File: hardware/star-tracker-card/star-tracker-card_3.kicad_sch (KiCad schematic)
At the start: 140 parts, among them J100 DM3BT-DSF-PEJS, J101 3-1734592-64-1734592-0, J3 CONN_03LONGPADS, U11 TCAN330, U17 25AAXX, U3 THGBMJG7C2LBAU8, U5 SN74LVC8T245MPWREPPW24-M, U6 CLVCH16T245MDGGREP, U7 OSD3358-512M-BSM, U8 TLV70028QDDCRQ1, U9 TCA9509DGKRDGK8-M

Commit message: More EAGLE import cleanup
Fixed sheets, did some ERC cleanup, imported into layout, impmorted 4 layer DRC rules.
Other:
- note removed: "1.2"
- note removed: "OreSat Star Tracker: Camera, eMMC"
- company: (none) -> Portland State Aerospace Society
- title: (none) -> OreSat Star Tracker

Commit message: Schematic Overhaul of v1.3
Changed schematic to hierarchical, changed debug connector, updated OPD, removed JTAG, and ESD protection on removed connectors
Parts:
- removed C16, C17, C20, C21, C24, C25, C26, C28: 0.1uF, star-tracker-card:.0603-A, symbol star-tracker-card-eagle-import:C-EU0603-A
- removed C23, C27: 1uF, star-tracker-card:.0603-A, symbol star-tracker-card-eagle-import:C-EU0603-A
- removed C42, C43: 22uF, star-tracker-card:C1210, symbol star-tracker-card-eagle-import:C-EUC1210
- removed J101: 3-1734592-64-1734592-0, star-tracker-card:TE_3-1734592-6, symbol star-tracker-card-eagle-import:3-1734592-64-1734592-0
- removed J3: CONN_03LONGPADS, star-tracker-card:1X03_LONGPADS, symbol star-tracker-card-eagle-import:CONN_03LONGPADS
- removed JP105, JP106, JP108, JP109: JUMPER-SMT_3_1-NC_TRACE_SILK, star-tracker-card:SMT-JUMPER_3_1-NC_TRACE_SILK, symbol star-tracker-card-eagle-import:JUMPER-SMT_3_1-NC_TRACE_SILK
- removed JP107: JUMPER-SMT_3_NO_SILK, star-tracker-card:SMT-JUMPER_3_NO_SILK, symbol star-tracker-card-eagle-import:JUMPER-SMT_3_NO_SILK
- removed R11, R12, R14, R16, R21: 10k, star-tracker-card:.0603-A, symbol star-tracker-card-eagle-import:R-US_0603-A
- removed R17, R18: 4.7k, star-tracker-card:.0603-A, symbol star-tracker-card-eagle-import:R-US_0603-A
- removed R24, R25, R26: 100K, star-tracker-card:ARRAY_EXBA-M, symbol star-tracker-card-eagle-import:EXB-A10P391JC_ARRAY_EXBA-M
- removed TP10, TP11, TP113, TP116, TP119, TP12, TP13, TP135, TP137, TP143, TP147, TP148, TP149, TP15, TP152, TP153, TP158, TP159, TP16, TP162, TP17, TP174, TP18, TP19, TP20, TP21, TP23, TP24, TP26, TP27, TP28, TP29, TP36, TP37, TP5, TP6, TP7, TP8, TP9: TEST-POINT3X4, star-tracker-card:PAD.03X.04, symbol star-tracker-card-eagle-import:TEST-POINT3X4
- removed U5: SN74LVC8T245MPWREPPW24-M, star-tracker-card:PW24-M, symbol star-tracker-card-eagle-import:SN74LVC8T245MPWREPPW24-M
- removed U6: CLVCH16T245MDGGREP, star-tracker-card:DGG48-M, symbol star-tracker-card-eagle-import:CLVCH16T245MDGGREP
- removed unit 4 of U7
- removed U8: TLV70028QDDCRQ1, star-tracker-card:SOT23-5, symbol star-tracker-card-eagle-import:TLV70028QDDCRQ1
- removed U9: TCA9509DGKRDGK8-M, star-tracker-card:DGK8-M, symbol star-tracker-card-eagle-import:TCA9509DGKRDGK8-M
- C10, C11, C12, C3, C31, C40, C5, C6, C9: footprint star-tracker-card:.0603-A -> oresat-passives:c_0603-SMALL; symbol star-tracker-card-eagle-import:C-EU0603-A -> Device:C_Small
- C2: footprint star-tracker-card:.0805-B -> oresat-passives:0805-B-NOSILK; symbol star-tracker-card-eagle-import:C-EU0805-B -> Device:C_Small
- C8: footprint star-tracker-card:.0805-B -> oresat-passives:0805-B-NOSILK
- D2, D3, D4, D5: symbol star-tracker-card-eagle-import:LED-BLUE0603 -> Device:LED
- R2, R29, R3, R30, R4, R5, R60: footprint star-tracker-card:.0603-A -> Resistor_SMD:R_0603_1608Metric; symbol star-tracker-card-eagle-import:R-US_0603-A -> Device:R_Small_US
- R59: footprint star-tracker-card:.0603-A -> Resistor_SMD:R_0603_1608Metric; symbol star-tracker-card-eagle-import:R-US_0603-A -> Device:R_Small_US; now not fitted
- TP100, TP101, TP103, TP104, TP105, TP106, TP107, TP108, TP111, TP114, TP115, TP117, TP118, TP120, TP122, TP123, TP124, TP125, TP126, TP127, TP128, TP131, TP134, TP142, TP146, TP177, TP178, TP180, TP22, TP30, TP35, TP40, TP69: footprint star-tracker-card:PAD.03X.04 -> oresat-misc:TestPoint_Pad_D1.0mm; symbol star-tracker-card-eagle-import:TEST-POINT3X4 -> oresat-misc:Test-Point-1mm-round; now left out of the parts list
- U11: footprint star-tracker-card:SOT23-8_TI-DCN -> oresat-live-card:SOT23-8_TI-DCN; symbol star-tracker-card-eagle-import:TCAN330 -> oresat-ics:TCAN330; Distributor (none) -> DigiKey; MPN (none) -> TCAN330GDCN
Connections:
- net GND: now also D2.1 (K), D3.1 (K), D4.1 (K), D5.1 (K); no longer D2.C, D3.C, D4.C, D5.C
- net UART0_RX: now also TP146.1; no longer TP146.P$1 (1)
- net UART0_TX: now also TP142.1; no longer TP142.P$1 (1)
- net at R2.2: now also D2.2 (A); no longer D2.A
- net at U7.N1 (GPMC_OEN_REN): now also TP128.1; no longer TP128.P$1 (1)
- net at U7.P15 (GPMC_WAIT0): now also TP114.1; no longer TP114.P$1 (1)
- net at U7.T15 (GPMC_A9): now also TP108.1; no longer TP108.P$1 (1)
- net at U7.N14 (GPMC_BEN1): now also TP125.1; no longer TP125.P$1 (1)
- net at U7.A4 (XDMA_EVENT_INTR0): now also TP30.1; no longer TP30.P$1 (1)
- net at U7.C12 (UART0_CTSN): now also TP177.1; no longer TP177.P$1 (1)
- net at U7.C13 (UART0_RTSN): now also TP178.1; no longer TP178.P$1 (1)
- net at J100.CD (CD#), R8.6 (66), U7.C14 (SPI0_CS1): now also TP22.1; no longer TP22.P$1 (1)
- net at U7.C5 (ECAP0_IN_PWM0_OUT): now also TP180.1; no longer TP180.P$1 (1)
- net at U7.M1 (GPMC_ADVN_ALE): now also TP134.1; no longer TP134.P$1 (1)
- net at U7.N2 (GPMC_WEN): now also TP127.1; no longer TP127.P$1 (1)
- net at U7.N3 (GPMC_BEN0_CLE): now also TP131.1; no longer TP131.P$1 (1)
- net at U7.P12 (GPMC_A2): now also TP126.1; no longer TP126.P$1 (1)
- net at U7.P3 (GPMC_CSN0): now also TP122.1; no longer TP122.P$1 (1)
- net at U7.P5 (GPMC_AD9): now also TP123.1; no longer TP123.P$1 (1)
- net at U7.P6 (GPMC_AD12): now also TP124.1; no longer TP124.P$1 (1)
- net at U7.R12 (GPMC_A1): now also TP118.1; no longer TP118.P$1 (1)
- net at U7.R15 (GPMC_A10): now also TP117.1; no longer TP117.P$1 (1)
- net at U7.R16 (GPMC_WPN): now also TP111.1; no longer TP111.P$1 (1)
- net at U7.R5 (GPMC_AD10): now also TP115.1; no longer TP115.P$1 (1)
- net at U7.R6 (GPMC_AD13): now also TP120.1; no longer TP120.P$1 (1)
- net at U7.R7 (GPMC_CSN3): now also TP107.1; no longer TP107.P$1 (1)
- net at U7.T12 (GPMC_A0): now also TP100.1; no longer TP100.P$1 (1)
- net at U7.T13 (GPMC_A3): now also TP101.1; no longer TP101.P$1 (1)
- net at U7.T16 (GPMC_A11): now also TP103.1; no longer TP103.P$1 (1)
- net at U7.T4 (GPMC_AD8): now also TP104.1; no longer TP104.P$1 (1)
- net at U7.T5 (GPMC_AD11): now also TP105.1; no longer TP105.P$1 (1)
- net at U7.T7 (GPMC_CLK): now also TP106.1; no longer TP106.P$1 (1)
- net at R4.2: now also D4.2 (A); no longer D4.A
- net at R3.2: now also D3.2 (A); no longer D3.A
- net at R5.2: now also D5.2 (A); no longer D5.A
- net at U11.5 (SHDN): now also TP35.1; no longer TP35.P$1 (1)
- net at U11.8 (S): now also TP40.1; no longer TP40.P$1 (1)
- net at U17.7 (~{HOLD}): now also TP69.1; no longer TP69.P$1 (1)
- net VSYNC_I renamed VSYNCI
- no-connect marks 11 -> 6
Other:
- note removed: "2.8V regulator"
- note removed: "36 Pin connector"
- note removed: "Boot SD SYSBOOT[4 : 0] == 0b11000 SPI0 -> MMC0 -> USB0 -> UART0 Boot eMMC SYSBOOT[4 : 0] == 0b11100 MMC1 -> MMC0 -> UART0 -> USB0"
- note removed: "Camera Control Level Shifter"
- note removed: "Camera Output Level Shifter"
- note removed: "Default Sysboot Pins SYSBOOT[4 : 0] == 0b11x00 SYSBOOT[2] HIGH == eMMC SYSBOOT[2] LOW == SD Card"
- note removed: "GPIO -> PIN map gpio3_9 == mii1_tx_clk gpio0_28 == mii1_txd0 gpio0_21 == mii1_txd1 gpio0_17 == mii1_txd2 gpio0_16 == mii1_txd3 gpio3_3 == mii1_tx_en gpio3_1 == mii1_crs gpio3_0 == mii1_col gpio3_10 == mii1_rx_clk gpio2_21 == mii1_rxd0 gpio2_20 == mii1_rxd1 gpio2_19 == mii1_rxd2 gpio2_18 == mii1_rxd3 gpio3_2 == mii1_rx_er gpio3_4 == mii1_rx_dv gpio0_0 == mdio"
- note removed: "I2C Transceiver"
- note removed: "NOTE: All these signals are outputs with the exception of FLASH. Likewise, I put the outputs on GPIO2,3 and inputs on GPIO0. I am not sure if this is better, but it seemed logical"
- note removed: "OE pullup to start in high Z"
- note removed: "SYSBOOT Circuit"
- note removed: "SYSBOOT Jumper to config boot order must use very light pullups because boot config is latched at boot and then the pins a used for other purposes"
- note removed: "SYSBOOT[15 : 5] == 0b0100_0000_000"
- note removed: "These pullups can be populated instead of the optional ones on the camera board"
- moved on the sheet: C8, JP102, JP103, JP110, JP111, R10, R8, R9

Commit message: Update
Update to the octavo schematic
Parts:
- removed JP102, JP103, JP110, JP111: JUMPER-SMT_3_1-NC_TRACE_SILK, star-tracker-card:SMT-JUMPER_3_1-NC_TRACE_SILK, symbol star-tracker-card-eagle-import:JUMPER-SMT_3_1-NC_TRACE_SILK
- C8: symbol star-tracker-card-eagle-import:C-EU0805-B -> Device:C_Small
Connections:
- net D0_I: now also J100.2 (DAT3/CS), R8.2 (22), U7.C15 (MMC0_DAT3)
- net D1_I: now also J100.1 (DAT2), R8.9 (99), U7.C16 (MMC0_DAT2)
- net D2_I: now also J100.8 (DAT1), R8.4 (44), U7.A15 (MMC0_DAT1)
- net D3_I: now also J100.7 (DAT0/DO), R8.7 (77), U7.A16 (MMC0_DAT0)
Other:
- note removed: "SD Card Circuit pinout from RED board"
- moved on the sheet: C11

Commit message: DRC hunting
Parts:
- D2, D3, D4, D5: footprint star-tracker-card:LED-0603 -> LED_SMD:LED_0603_1608Metric
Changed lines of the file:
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@@
 			)
 		)
-		(property "Footprint" "star-tracker-card:LED-0603"
+		(property "Footprint" "LED_SMD:LED_0603_1608Metric"
 			(at 382.27 195.58 0)
 			(effects
@@
 			)
 		)
-		(property "Footprint" "star-tracker-card:LED-0603"
+		(property "Footprint" "LED_SMD:LED_0603_1608Metric"
 			(at 382.27 210.82 0)
 			(effects
@@
 			)
 		)
-		(property "Footprint" "star-tracker-card:LED-0603"
+		(property "Footprint" "LED_SMD:LED_0603_1608Metric"
 			(at 382.27 203.2 0)
 			(effects
@@
 			)
 		)
-		(property "Footprint" "star-tracker-card:LED-0603"
+		(property "Footprint" "LED_SMD:LED_0603_1608Metric"
 			(at 382.27 218.44 0)
 			(effects

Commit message: Big almost-done cleanup
Fixed a bunch of things in the schematic. Compared against C3 Octavo. Fixed all weird ERCs. Cleaned up a lot of planes on the layout. Moved uart switch, rerouted a bunch of traces for better layout. Fixed library issues, and board/sch sync issues.
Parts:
- removed C40: 0.1uF, oresat-passives:c_0603-SMALL, symbol Device:C_Small
- removed R59, R60: DNP, Resistor_SMD:R_0603_1608Metric, symbol Device:R_Small_US
- removed TP22, TP35, TP40, TP69: TEST-POINT3X4, oresat-misc:TestPoint_Pad_D1.0mm, symbol oresat-misc:Test-Point-1mm-round
- removed U17: 25AAXX, star-tracker-card:SOIC8, symbol star-tracker-card-eagle-import:25AAXX
- added TP1, TP14, TP2, TP31: TEST-POINT3X4, oresat-misc:TestPoint_Pad_D1.0mm, symbol oresat-misc:Test-Point-1mm-round
- C10, C12, C3, C5, C6, C9: value 1uF -> 1u; footprint oresat-passives:c_0603-SMALL -> oresat-passives:0603-C-NOSILK
- C11, C31: value 0.1uF -> 100n; footprint oresat-passives:c_0603-SMALL -> oresat-passives:0603-C-NOSILK
- C2, C8: value 10uF -> 10u
- D2, D3, D4, D5: value BLUE -> BLU; symbol Device:LED -> Device:LED_Small_Filled
- R2, R29, R3, R30, R4, R5: footprint Resistor_SMD:R_0603_1608Metric -> oresat-passives:0603-C-NOSILK
- U11: footprint oresat-live-card:SOT23-8_TI-DCN -> Package_TO_SOT_SMD:SOT-23-8; symbol oresat-ics:TCAN330 -> Interface_CAN_LIN:TCAN330
- U3: value THGBMJG7C2LBAU8 -> EMMC+RESET+5.1-COMPATIBLE-BA; footprint star-tracker-card:BGA-153(11.5X13)(EMMC-BA) -> oresat-ics:BGA-153(11.5X13)(EMMC-BA); symbol star-tracker-card-eagle-import:EMMC+RESET+5.1-COMPATIBLE-BA -> oresat-ics:EMMC+RESET+5.1-COMPATIBLE-BA
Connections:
- net GND: now also U3.A6 (VSSIO)
- net EMMC_CMD: now reaches R9.2 (22), U3.M5 (CMD), U7.P1 (GPMC_CSN2)
- net EMMC_D5: now reaches R9.3 (33), U3.B4 (D5), U7.T1 (GPMC_AD5)
- net EMMC_D4: now reaches R9.4 (44), U3.B3 (D4), U7.T2 (GPMC_AD4)
- net EMMC_D0: now reaches R9.6 (66), U3.A3 (D0), U7.R3 (GPMC_AD0)
- net EMMC_D3: now reaches R9.7 (77), U3.B2 (D3), U7.T3 (GPMC_AD3)
- net EMMC_SCK: now reaches R9.8 (88), U3.M6 (SCK), U7.P2 (GPMC_CSN1)
- net CAN1_TXD: now reaches U11.1 (TXD), U7.A11 (UART1_RXD)
- net at U7.A13 (SPI0_SCLK): now also TP1.1
- net at U7.A14 (SPI0_CS0): now also TP31.1
- net CAN1_RXD: now reaches U11.4 (RXD), U7.B11 (UART1_TXD)
- net at U7.B13 (SPI0_D0): now also TP2.1
- net at U7.B14 (SPI0_D1): now also TP14.1
- net MMC1_CLK: now reaches J100.5 (CLK), R8.3 (33), U7.B15 (MMC0_CLK)
- net MMC1_CMD: now reaches J100.3 (CMD/DI), R8.8 (88), U7.B16 (MMC0_CMD)
- net MMC1_CD: now reaches J100.CD (CD#), R8.6 (66), U7.C14 (SPI0_CS1)
- net EMMC_D6: now reaches R10.8 (88), U3.B5 (D6), U7.P4 (GPMC_AD6)
- net EMMC_D2: now reaches R10.9 (99), U3.A5 (D2), U7.R1 (GPMC_AD2)
- net EMMC_nRST: now reaches R10.3 (33), U3.K5 (~{RST}), U7.R13 (GPMC_A4)
- net EMMC_D1: now reaches R10.1 (11), U3.A4 (D1), U7.R2 (GPMC_AD1)
- net EMMC_D7: now reaches R10.2 (22), U3.B6 (D7), U7.R4 (GPMC_AD7)
- no-connect marks 6 -> 8
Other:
- note added: "0805"
- note added: "All resistors are 0603 1% AEC-Q200 unless marked. All capacitors are 0603 AEC-Q200 Vw >= 16V X5R or better unless marked."
- note added: "Need ~2.2uF, using two 1uF for simplicity"
- note removed: "CAN Transceiver"
- note removed: "CAN1 RX --> B11 --> UART1_TXD CAN1 TX --> A11 --> UART1_RXD"
- note removed: "Camera Connector and Circuitry"
- note removed: "I2C2 SCL == UART1_RTSN == A10 I2C2 SDA == UART1_CTSN == B10"
- note removed: "Need ~2.2uF here, but using two 1uF for simplicity"
- note removed: "SPI Flash/EEPROM For SPI boot DNP for now"
- moved on the sheet: C10, C11, C12, C2, C3, C31, C5, C6, C8, C9, J100, R10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

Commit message: BOM 99% completed, push for final review
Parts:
- C10, C12, C3, C5, C6, C9: DIS (none) -> DigiKey; DPN (none) -> 490-GRT188R71E105KE13DCT-ND; MFR (none) -> Murata Electronics; MPN (none) -> GRT188R71E105KE13D
- C11, C31: DIS (none) -> DigiKey; DPN (none) -> 399-6856-1-ND; MFR (none) -> KEMET; MPN (none) -> C0603C104K5RACAUTO
- C2, C8: DIS (none) -> DigiKey; DPN (none) -> 490-GRT21BC71E106KE13KCT-ND; MFR (none) -> Murata Electronics; MPN (none) -> GRT21BC71E106KE13K
- D2, D3, D4, D5: DIS (none) -> DigiKey; DPN (none) -> 732-4966-1-ND; MFR (none) -> Wurth; MPN (none) -> 150060BS75000
- J100: DIS (none) -> DigiKey; DPN (none) -> HR1942CT-ND; MFR (none) -> Hirose; MPN (none) -> DM3BT-DSF-PEJS
- R10, R8, R9: DIS (none) -> DigiKey; DPN U7103CT-ND -> RMCF0603FT10K0CT-ND; MFR (none) -> Stackpole Electronics; MPN EXB-A10P103J -> RMCF0603FT10K0
- R2, R3, R4, R5: DIS (none) -> DigiKey; DPN (none) -> RMCF0603FT2K70CT-ND; MFR (none) -> Stackpole Electronics; MPN (none) -> RMCF0603FT1K00
- R29, R30: DIS (none) -> DigiKey; DPN (none) -> RMCF0603FT4K70CT-ND; MFR (none) -> Stackpole Electronics; MPN (none) -> RMCF0603FT4K70
- U11: DIS (none) -> DigiKey; DPN (none) -> 296-44211-1-ND; MFR (none) -> Texas Instruments
- U3: DIS (none) -> DigiKey; DPN THGBMJG7C2LBAU8-ND -> 1052-SFEM016GB1EA1TO-I-GE-121-STD-ND; MFR (none) -> Swissbit; MPN THGBMJG7C2LBAU8 -> SFEM016GB1EA1TO-I-GE-121-STD
- U7: DIS (none) -> DigiKey; DPN (none) -> 1676-OSD3358-1G-ISM-ND; MFR (none) -> Octavo Systems LLC; MPN (none) -> OSD3358-1G-ISM

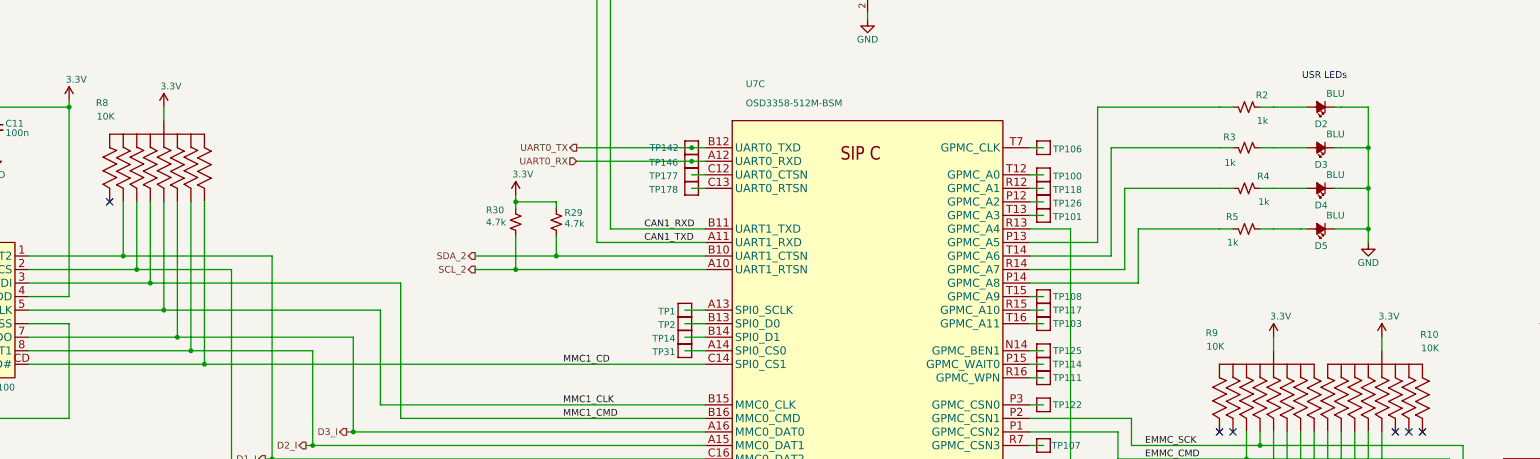
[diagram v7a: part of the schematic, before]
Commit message: Star Tracker v1.3 files, including new Makefile, Readme, and fixes in ERC, DRC, and layout
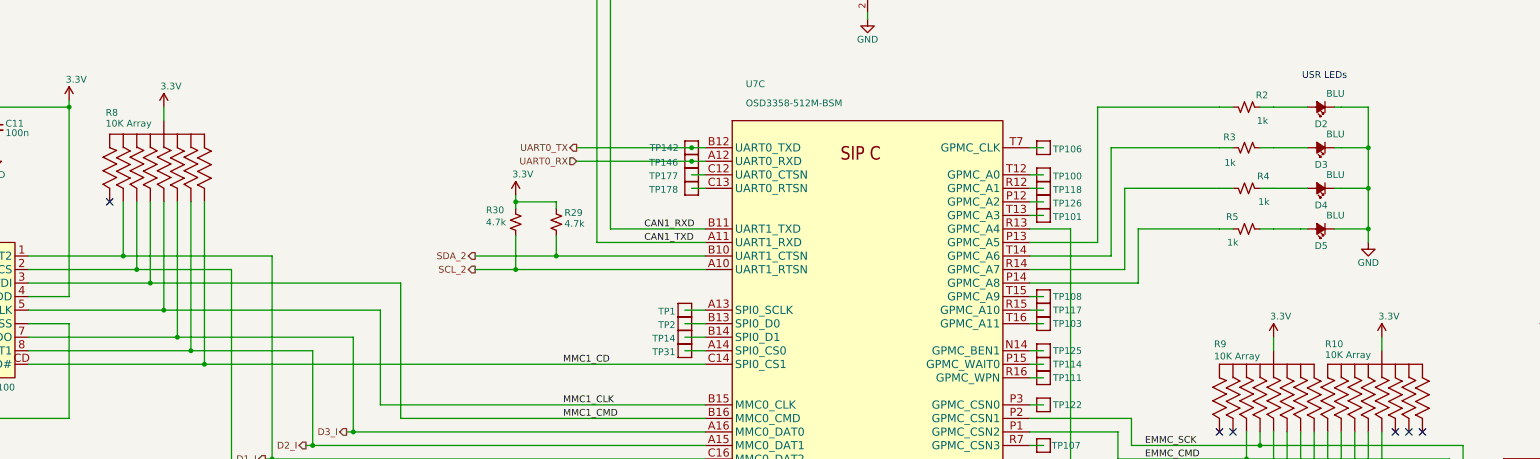
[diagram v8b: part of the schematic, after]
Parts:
- R10, R8, R9: value 10K -> 10K Array; DPN RMCF0603FT10K0CT-ND -> U7103CT-ND; MFR Stackpole Electronics -> Panasonic Electronic Components; MPN RMCF0603FT10K0 -> EXB-A10P103J
- U11: Distributor DigiKey -> (none)
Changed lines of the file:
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@@
 	(title_block
 		(title "OreSat Star Tracker")
-		(date "2026-04-15")
+		(date "2026-04-22")
 		(rev "1.3")
 		(company "Portland State Aerospace Society")
@@
 		(dnp no)
 		(property "Reference" "R9"
-			(at 275.5392 126.9492 90)
+			(at 277.114 129.032 90)
 			(show_name no)
 			(do_not_autoplace no)
@@
 			)
 		)
-		(property "Value" "10K"
-			(at 275.6916 129.4892 90)
+		(property "Value" "10K Array"
+			(at 277.114 131.318 90)
 			(show_name no)
 			(do_not_autoplace no)
@@
 			)
 		)
-		(property "Datasheet" "https://www.seielect.com/catalog/SEI-RMCF_RMCP.pdf"
+		(property "Datasheet" "https://industrial.panasonic.com/ww/products/pt/resistor-network-array/models/EXBA10P103J"
 			(at 278.13 132.08 0)
 			(hide yes)
@@
 			)
 		)
-		(property "Description" "10 kOhms ±1% 0.1W, 1/10W Chip Resistor 0603 (1608 Metric) Automotive AEC-Q200 Thick Film"
+		(property "Description" "10k Ohm ±5% 62.5mW Power Per Element Bussed 8 Resistor Network/Array ±200ppm/°C 2512 (6432 Metric), Concave, Long Side Terminals"
 			(at 278.13 132.08 0)
 			(hide yes)
@@
 			)
 		)
-		(property "DPN" "RMCF0603FT10K0CT-ND"
+		(property "DPN" "U7103CT-ND"
 			(at 278.13 132.08 0)
 			(hide yes)
@@
 			)
 		)
-		(property "MPN" "RMCF0603FT10K0"
+		(property "MPN" "EXB-A10P103J"
 			(at 278.13 132.08 0)
 			(hide yes)
@@
 			)
 		)
-		(property "MFR" "Stackpole Electronics"
+		(property "MFR" "Panasonic Electronic Components"
 			(at 278.13 132.08 90)
 			(hide yes)
@@
 		(dnp no)
 		(property "Reference" "R8"
-			(at 67.2592 83.7692 90)
+			(at 69.088 85.598 90)
 			(show_name no)
 			(do_not_autoplace no)
@@
 			)
 		)
-		(property "Value" "10K"
-			(at 67.4116 86.3092 90)
+		(property "Value" "10K Array"
+			(at 69.088 87.63 90)
 			(show_name no)
 			(do_not_autoplace no)
@@
 			)
 		)
-		(property "Datasheet" "https://www.seielect.com/catalog/SEI-RMCF_RMCP.pdf"
+		(property "Datasheet" "https://industrial.panasonic.com/ww/products/pt/resistor-network-array/models/EXBA10P103J"
 			(at 69.85 88.9 0)
 			(hide yes)
@@
 			)
 		)
-		(property "Description" "10 kOhms ±1% 0.1W, 1/10W Chip Resistor 0603 (1608 Metric) Automotive AEC-Q200 Thick Film"
+		(property "Description" "10k Ohm ±5% 62.5mW Power Per Element Bussed 8 Resistor Network/Array ±200ppm/°C 2512 (6432 Metric), Concave, Long Side Terminals"
 			(at 69.85 88.9 0)
 			(hide yes)
@@
 			)
 		)
-		(property "DPN" "RMCF0603FT10K0CT-ND"
+		(property "DPN" "U7103CT-ND"
 			(at 69.85 88.9 0)
 			(hide yes)
@@
 			)
 		)
-		(property "MPN" "RMCF0603FT10K0"
+		(property "MPN" "EXB-A10P103J"
 			(at 64.77 91.948 0)
 			(hide yes)
@@
 			)
 		)
-		(property "MFR" "Stackpole Electronics"
+		(property "MFR" "Panasonic Electronic Components"
 			(at 69.85 88.9 90)
 			(hide yes)
@@
 			)
 		)
-		(property "Distributor" "DigiKey"
-			(at 212.09 55.88 0)
-			(hide yes)
-			(show_name no)
-			(do_not_autoplace no)
-			(effects
-				(font
-					(size 1.27 1.27)
-				)
-			)
-		)
 		(property "MPN" "TCAN330GDCN"
 			(at 212.09 55.88 0)
@@
 		(dnp no)
 		(property "Reference" "R10"
-			(at 315.8236 127.254 90)
+			(at 297.942 129.032 90)
 			(show_name no)
 			(do_not_autoplace no)
@@
 			)
 		)
-		(property "Value" "10K"
-			(at 315.976 129.794 90)
+		(property "Value" "10K Array"
+			(at 297.942 131.064 90)
 			(show_name no)
 			(do_not_autoplace no)
@@
 			)
 		)
-		(property "Datasheet" "https://www.seielect.com/catalog/SEI-RMCF_RMCP.pdf"
+		(property "Datasheet" "https://industrial.panasonic.com/ww/products/pt/resistor-network-array/models/EXBA10P103J"
 			(at 298.45 132.08 0)
 			(hide yes)
@@
 			)
 		)
-		(property "Description" "10 kOhms ±1% 0.1W, 1/10W Chip Resistor 0603 (1608 Metric) Automotive AEC-Q200 Thick Film"
+		(property "Description" "10k Ohm ±5% 62.5mW Power Per Element Bussed 8 Resistor Network/Array ±200ppm/°C 2512 (6432 Metric), Concave, Long Side Terminals"
 			(at 298.45 132.08 0)
 			(hide yes)
@@
 			)
 		)
-		(property "DPN" "RMCF0603FT10K0CT-ND"
+		(property "DPN" "U7103CT-ND"
 			(at 298.45 132.08 0)
 			(hide yes)
@@
 			)
 		)
-		(property "MPN" "RMCF0603FT10K0"
+		(property "MPN" "EXB-A10P103J"
 			(at 298.45 132.08 0)
 			(hide yes)
@@
 			)
 		)
-		(property "MFR" "Stackpole Electronics"
+		(property "MFR" "Panasonic Electronic Components"
 			(at 298.45 132.08 90)
 			(hide yes)
